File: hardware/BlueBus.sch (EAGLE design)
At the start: 77 parts, among them Y1 8MHz, Y2 32.768kHz

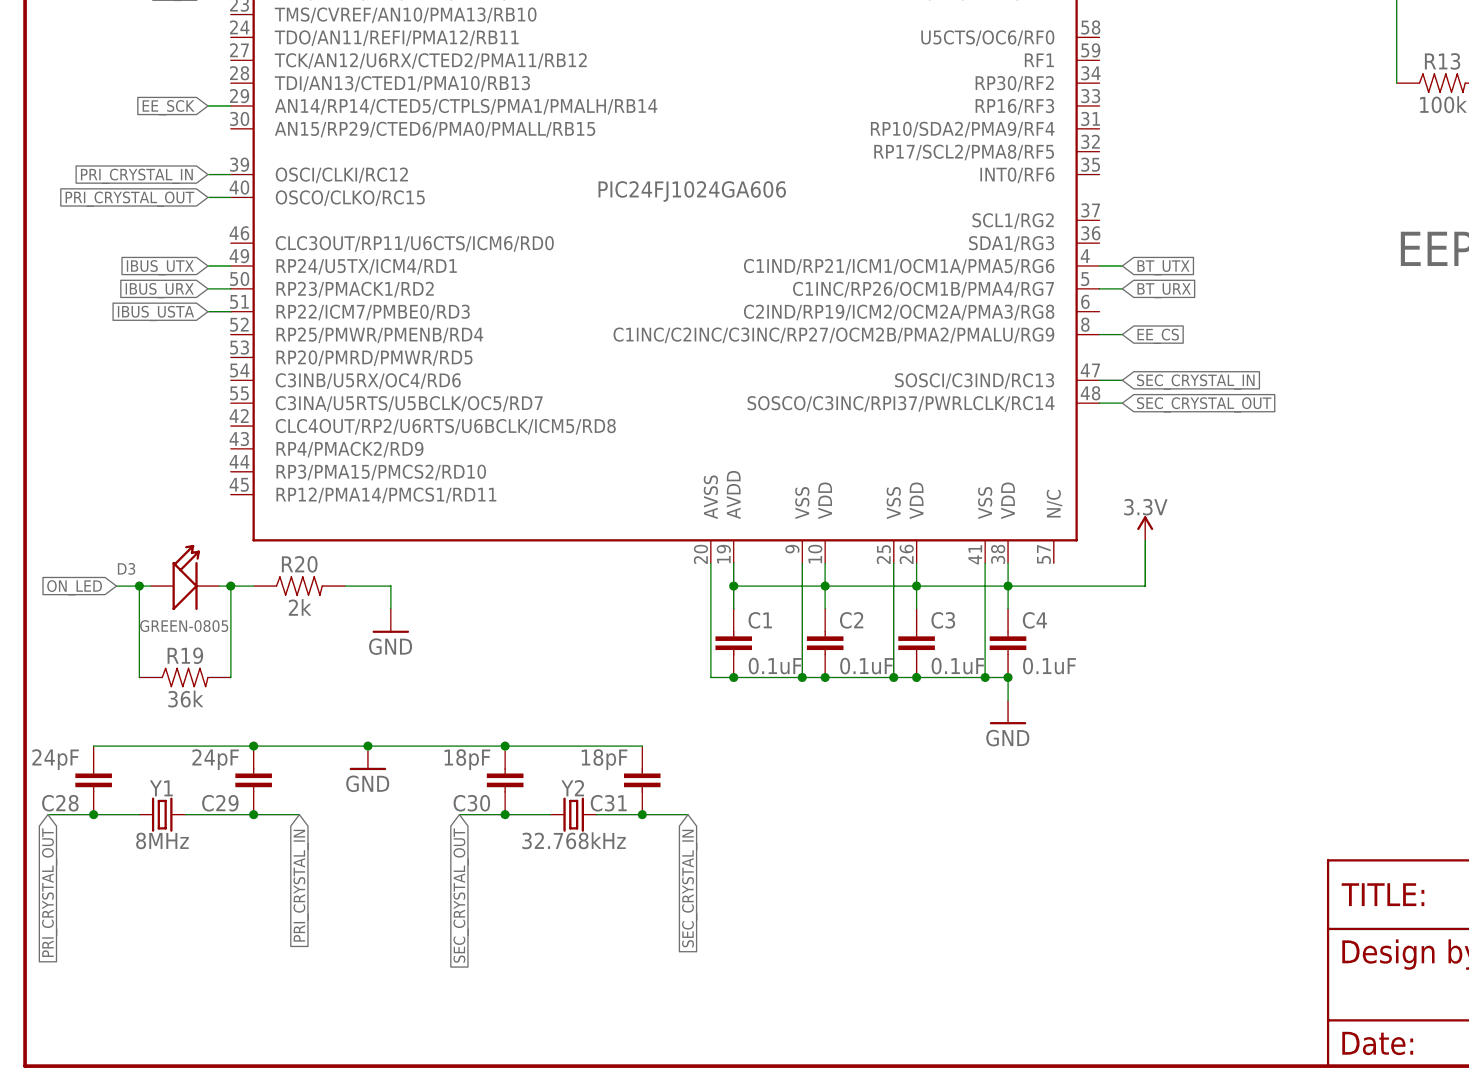
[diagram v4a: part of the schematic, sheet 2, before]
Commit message: [ADD] hardware: BlueBus v5 updates * Remove external crystals * Add pull up resistors to MCLR -- Bug in existing boards causing unstable operation * Rewire BC127 UART lines to MCU
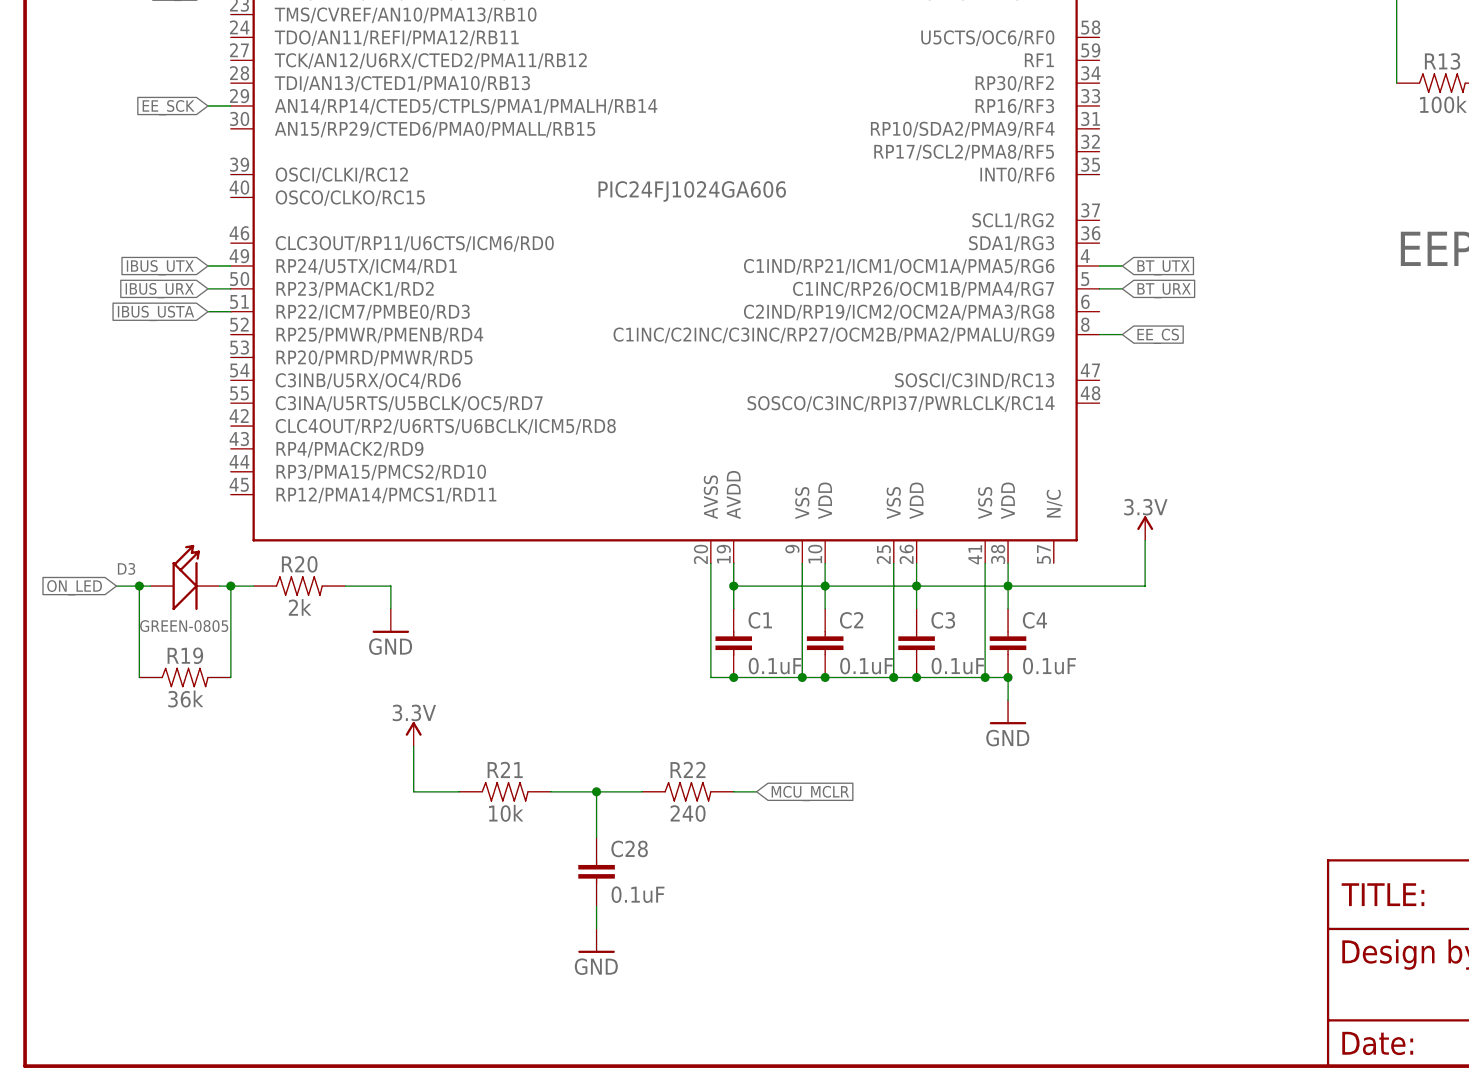
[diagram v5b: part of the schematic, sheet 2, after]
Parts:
- removed C29: 24pF, Passives:24PF
- removed C30, C31: 18pF, Passives:18PF
- removed Y1: 8MHz, Passives:CRYSTAL-8MHZ
- removed Y2: 32.768kHz, Passives:CRYSTAL-32.768KHZSMD-3.2X1.5
- added R21: 10k, Passives:10KOHM0805
- added R22: 240, Passives:240OHM
- C28: value 24pF -> 0.1uF; device Passives:24PF -> Passives:0.1UF
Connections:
- removed net PRI_CRYSTAL_IN: C29.1, PIC24FJ1024GA606.OSCI/CLKI/RC12, Y1.2
- removed net PRI_CRYSTAL_OUT: C28.1, PIC24FJ1024GA606.OSCO/CLKO/RC15, Y1.1
- removed net SEC_CRYSTAL_IN: C31.1, PIC24FJ1024GA606.SOSCI/C3IND/RC13, Y2.2
- removed net SEC_CRYSTAL_OUT: C30.1, PIC24FJ1024GA606.SOSCO/C3INC/RPI37/PWRLCLK/RC14, Y2.1
- new net MCU_MCLR_PULL_UP: C28.1, R21.2, R22.1
- net 3.3V: now also R21.1
- net GND: no longer C29.2, C30.2, C31.2
- net MCU_MCLR: now also R22.2
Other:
- moved on the sheet: C28

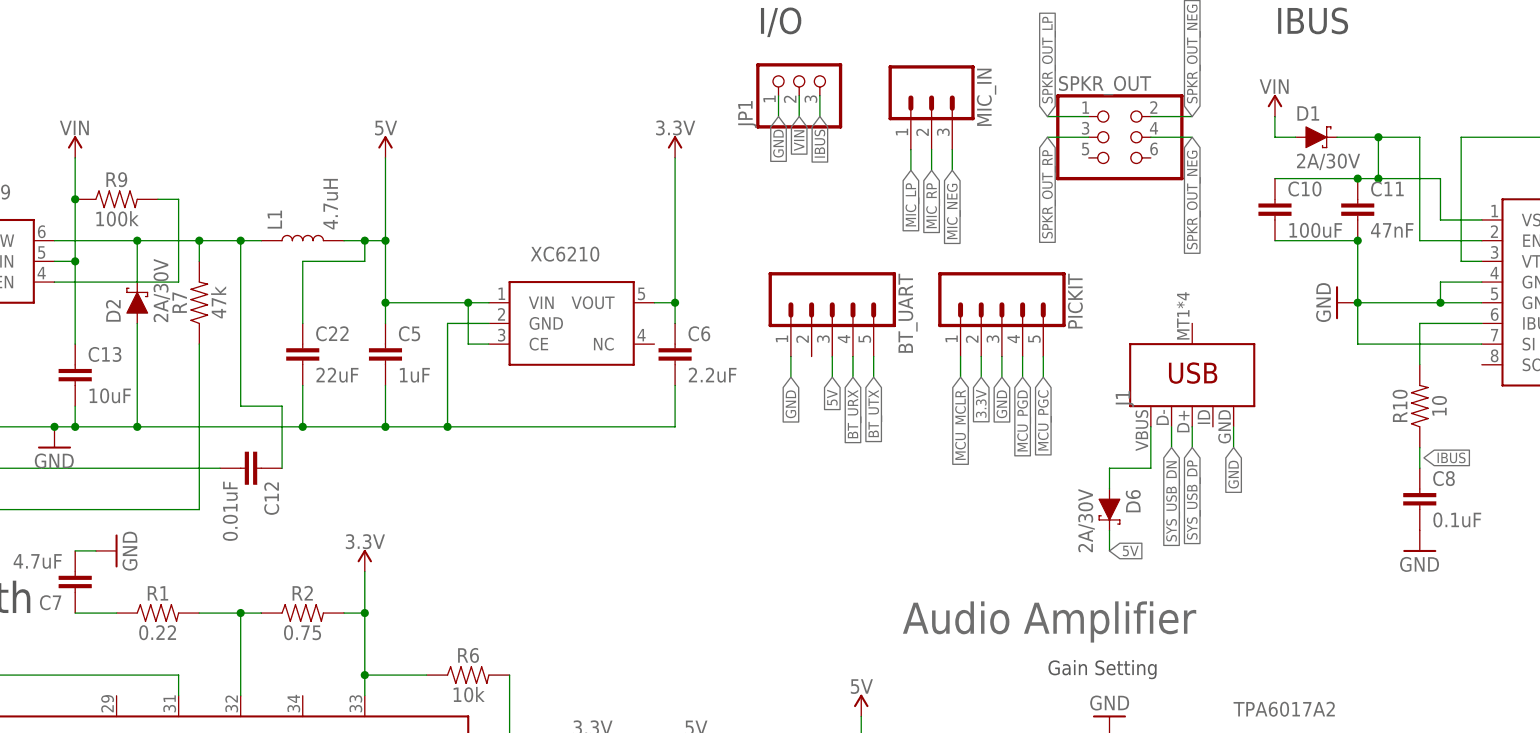
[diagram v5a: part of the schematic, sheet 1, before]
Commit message: [ADD] hardware: BlueBus BOM Updates * Add GitHub link to Silkscreen * Update Embedded BOM
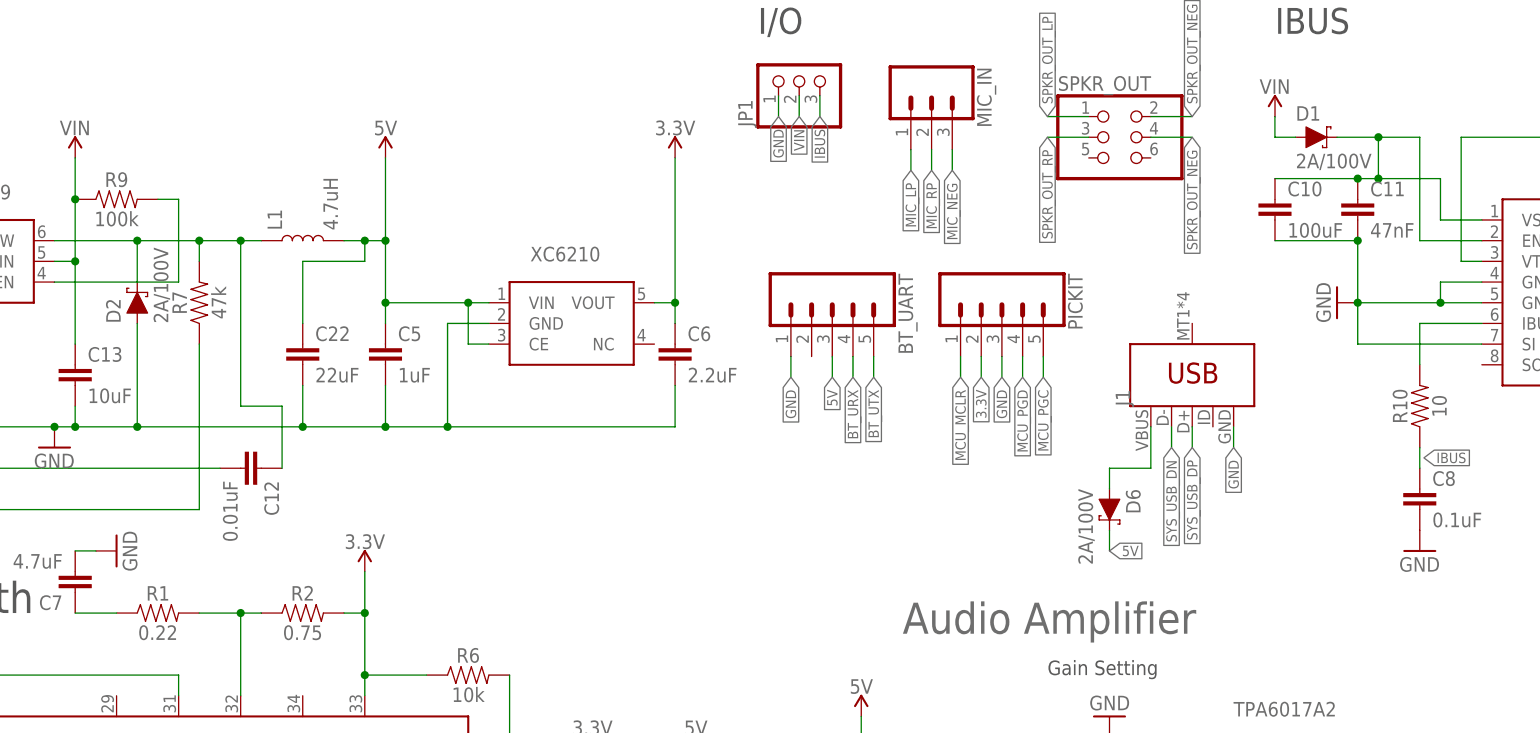
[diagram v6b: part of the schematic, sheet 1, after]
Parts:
- D1, D2, D6: value 2A/30V -> 2A/100V
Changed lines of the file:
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@@
 <part name="GND1" library="supply1" library_urn="urn:adsk.eagle:library:371" deviceset="GND" device=""/>
 <part name="GND10" library="supply1" library_urn="urn:adsk.eagle:library:371" deviceset="GND" device=""/>
-<part name="D2" library="Passives" deviceset="SCHOTTKYDIODE2A30V" device="" value="2A/30V"/>
+<part name="D2" library="Passives" deviceset="SCHOTTKYDIODE2A30V" device="" value="2A/100V"/>
 <part name="L1" library="Passives" deviceset="MPLC0730L4R7" device="" value="4.7uH"/>
 <part name="MCP2221A" library="ICs" deviceset="MCP2221A" device="" value=""/>
@@
 <part name="R7" library="Passives" deviceset="47KOHM" device="" value="47k"/>
 <part name="J1" library="SparkFun-Connectors" library_urn="urn:adsk.eagle:library:513" deviceset="USB_MICRO-B" device="_SMT" package3d_urn="urn:adsk.eagle:package:38240/1"/>
-<part name="D6" library="Passives" deviceset="SCHOTTKYDIODE2A30V" device="" value="2A/30V"/>
-<part name="D1" library="Passives" deviceset="SCHOTTKYDIODE2A30V" device="" value="2A/30V"/>
+<part name="D6" library="Passives" deviceset="SCHOTTKYDIODE2A30V" device="" value="2A/100V"/>
+<part name="D1" library="Passives" deviceset="SCHOTTKYDIODE2A30V" device="" value="2A/100V"/>
 <part name="C10" library="Passives" deviceset="100UF" device="2917" value="100uF"/>
 <part name="C11" library="Passives" deviceset="47NF" device="" value="47nF"/>
